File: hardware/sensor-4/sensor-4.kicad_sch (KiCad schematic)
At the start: 13 parts, among them J101 2x05_Horizontal, U101 A31010SEHALT-10

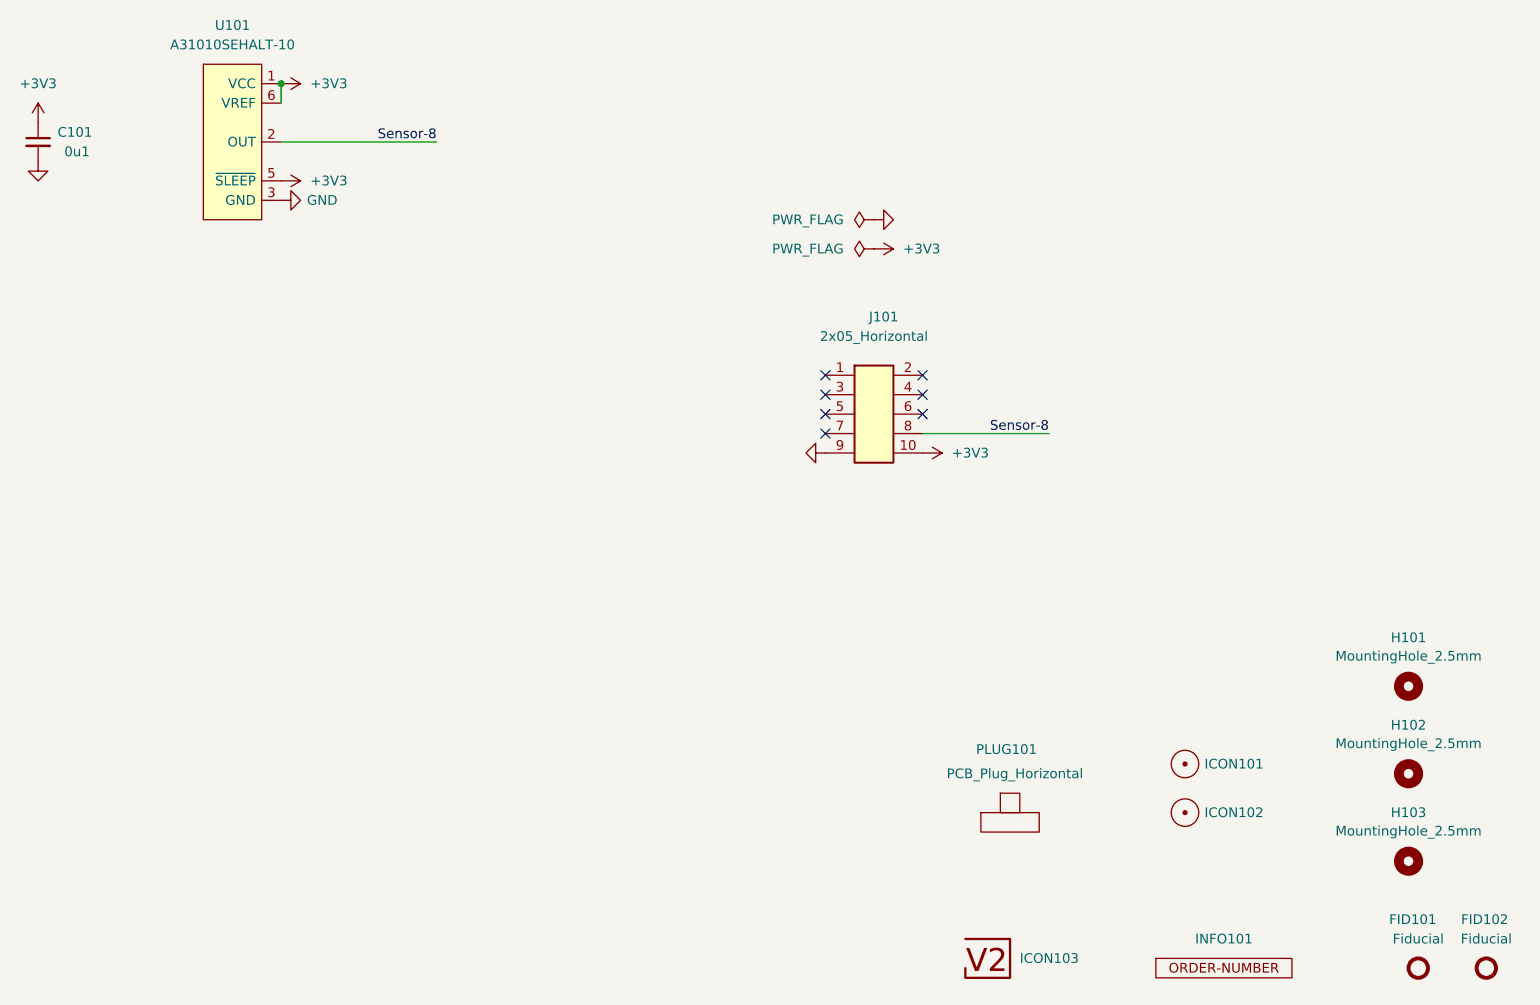
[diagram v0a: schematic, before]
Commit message: Replace Order_Number
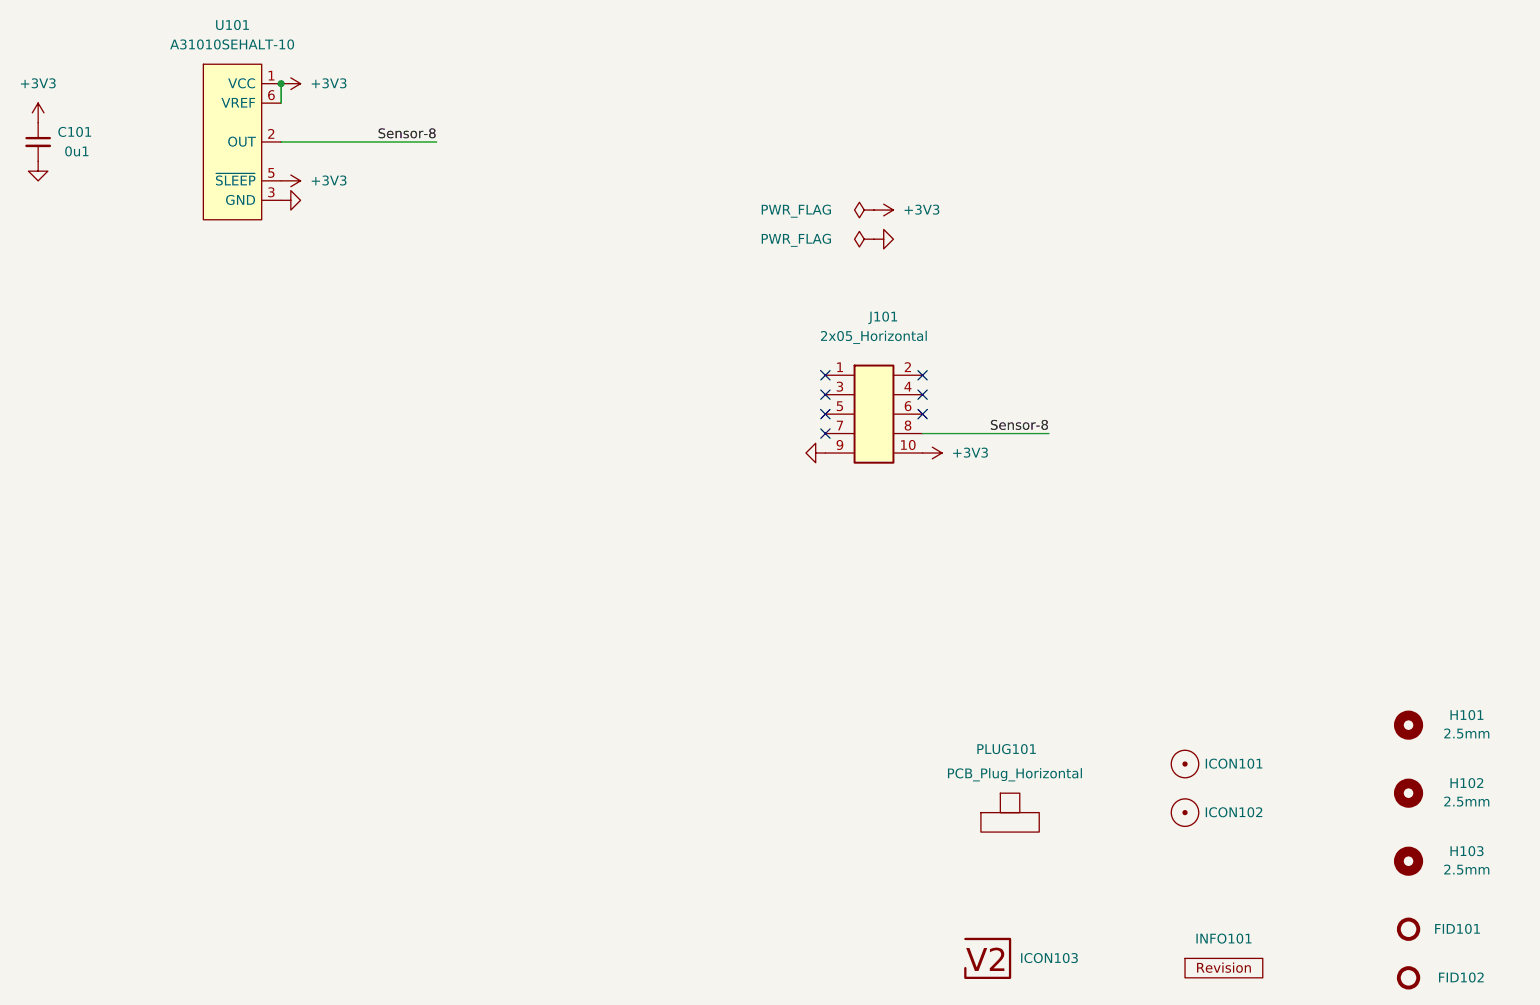
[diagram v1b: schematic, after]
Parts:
- C101: footprint Capacitor_SMD:C_0603_1608Metric -> V2_Capacitor_SMD:C_0603; symbol Device:C_Small -> V2_Device:C_0603_0u1; Manufacturer (none) -> TDK; Mouser (none) -> 810-CGA3E2X7R1H104MA; Product (none) -> CGA3E2X7R1H104M080AA; Rating (none) -> 50V
- FID101, FID102: value Fiducial -> Fiducial_Paste
- H101, H102, H103: value MountingHole_2.5mm -> 2.5mm
- INFO101: value ORDER-NUMBER -> ~; footprint V2_Production:Order_Number -> V2_Production:Revision; symbol V2_Production:Order_Number -> V2_Production:Revision
- J101: Manufacturer (none) -> Amphenol FCI; Mouser (none) -> 649-200211120001T4LF; Product (none) -> 20021112-00010T4LF
- U101: Manufacturer (none) -> Allegro MicroSystems; Mouser (none) -> 250-A31010SEHALT-10; Product (none) -> A31010SEHALT-10
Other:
- moved on the sheet: FID101, FID102, H101, H102

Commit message: Update Library
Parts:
- C101: symbol V2_Device:C_0603_0u1 -> V2_Capacitor:0603_0u1
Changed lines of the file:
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@@
 		(dnp no)
 		(fields_autoplaced yes)
-		(property "Reference" "#PWR0107"
+		(property "Reference" "#PWR107"
 			(at 190.5 76.2 0)
 			(effects
@@
 			(project ""
 				(path "/6c8448b4-b04d-47e1-934e-e40cbe27a7be"
-					(reference "#PWR0107")
+					(reference "#PWR107")
 					(unit 1)
 				)
@@
 		(dnp no)
 		(fields_autoplaced yes)
-		(property "Reference" "#PWR0109"
+		(property "Reference" "#PWR109"
 			(at 196.85 107.95 0)
 			(effects
@@
 			(project "sensor-1"
 				(path "/6c8448b4-b04d-47e1-934e-e40cbe27a7be"
-					(reference "#PWR0109")
+					(reference "#PWR109")
 					(unit 1)
 				)
@@
 		(dnp no)
 		(fields_autoplaced yes)
-		(property "Reference" "#PWR0102"
+		(property "Reference" "#PWR102"
 			(at 85.09 68.58 0)
 			(effects
@@
 			(project "sensor-1"
 				(path "/6c8448b4-b04d-47e1-934e-e40cbe27a7be"
-					(reference "#PWR0102")
+					(reference "#PWR102")
 					(unit 1)
 				)
@@
 		(on_board yes)
 		(dnp no)
-		(property "Reference" "#PWR0106"
+		(property "Reference" "#PWR106"
 			(at 200.66 80.01 0)
 			(effects
@@
 			(project "ring"
 				(path "/6c8448b4-b04d-47e1-934e-e40cbe27a7be"
-					(reference "#PWR0106")
+					(reference "#PWR106")
 					(unit 1)
 				)
@@
 		(dnp no)
 		(fields_autoplaced yes)
-		(property "Reference" "#PWR0104"
+		(property "Reference" "#PWR104"
 			(at 113.03 72.39 0)
 			(effects
@@
 			(project "sensor-1"
 				(path "/6c8448b4-b04d-47e1-934e-e40cbe27a7be"
-					(reference "#PWR0104")
+					(reference "#PWR104")
 					(unit 1)
 				)
@@
 	)
 	(symbol
-		(lib_id "V2_Device:C_0603_0u1")
+		(lib_id "V2_Capacitor:0603_0u1")
 		(at 85.09 67.31 0)
 		(unit 1)
@@
 		(on_board yes)
 		(dnp no)
-		(property "Reference" "#PWR0108"
+		(property "Reference" "#PWR108"
 			(at 181.61 107.95 0)
 			(effects
@@
 			(project "sensor-1"
 				(path "/6c8448b4-b04d-47e1-934e-e40cbe27a7be"
-					(reference "#PWR0108")
+					(reference "#PWR108")
 					(unit 1)
 				)
@@
 		(on_board yes)
 		(dnp no)
-		(property "Reference" "#PWR0103"
+		(property "Reference" "#PWR103"
 			(at 85.09 76.2 0)
 			(effects
@@
 			(project "sensor-1"
 				(path "/6c8448b4-b04d-47e1-934e-e40cbe27a7be"
-					(reference "#PWR0103")
+					(reference "#PWR103")
 					(unit 1)
 				)
@@
 		(on_board yes)
 		(dnp no)
-		(property "Reference" "#FLG0102"
+		(property "Reference" "#FLG102"
 			(at 194.31 74.295 0)
 			(effects
@@
 			(project "ring"
 				(path "/6c8448b4-b04d-47e1-934e-e40cbe27a7be"
-					(reference "#FLG0102")
+					(reference "#FLG102")
 					(unit 1)
 				)
@@
 		(on_board yes)
 		(dnp no)
-		(property "Reference" "#PWR0105"
+		(property "Reference" "#PWR105"
 			(at 123.19 74.93 0)
 			(effects
@@
 			(project "sensor-1"
 				(path "/6c8448b4-b04d-47e1-934e-e40cbe27a7be"
-					(reference "#PWR0105")
+					(reference "#PWR105")
 					(unit 1)
 				)
@@
 		(dnp no)
 		(fields_autoplaced yes)
-		(property "Reference" "#PWR0101"
+		(property "Reference" "#PWR101"
 			(at 113.03 59.69 0)
 			(effects
@@
 			(project "sensor-1"
 				(path "/6c8448b4-b04d-47e1-934e-e40cbe27a7be"
-					(reference "#PWR0101")
+					(reference "#PWR101")
 					(unit 1)
 				)
@@
 		(on_board yes)
 		(dnp no)
-		(property "Reference" "#FLG0101"
+		(property "Reference" "#FLG101"
 			(at 194.31 78.105 0)
 			(effects
@@
 			(project "ring"
 				(path "/6c8448b4-b04d-47e1-934e-e40cbe27a7be"
-					(reference "#FLG0101")
-					(unit 1)
-				)
+					(reference "#FLG101")
+					(unit 1)
+				)

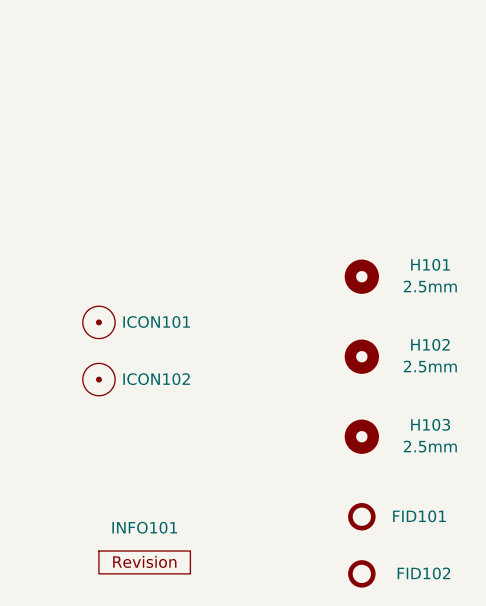
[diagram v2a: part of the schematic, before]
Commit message: KiCad 10
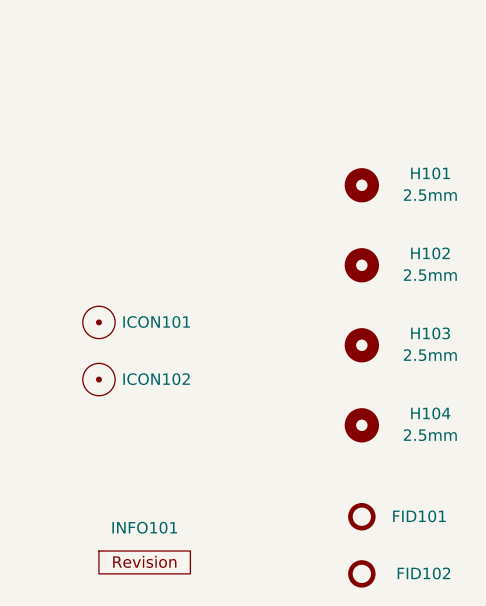
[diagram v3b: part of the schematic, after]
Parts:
- added H104: 2.5mm, V2_Mechanical:MountingHole_2.5mm, symbol V2_Mechanical:MountingHole_2.5mm
- INFO101: value ~ -> (none)
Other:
- moved on the sheet: H101, H102, H103

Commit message: Good Bye Imperial
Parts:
- C101: footprint V2_Capacitor_SMD:C_0603 -> V2_Capacitor_SMD:C_1608; symbol V2_Capacitor:0603_0u1 -> V2_Capacitor:1608_0u1
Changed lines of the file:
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@@
 	)
 	(symbol
-		(lib_id "V2_Capacitor:0603_0u1")
+		(lib_id "V2_Capacitor:1608_0u1")
 		(at 85.09 67.31 0)
 		(unit 1)
@@
 			)
 		)
-		(property "Footprint" "V2_Capacitor_SMD:C_0603"
+		(property "Footprint" "V2_Capacitor_SMD:C_1608"
 			(at 85.09 67.31 0)
 			(hide yes)
